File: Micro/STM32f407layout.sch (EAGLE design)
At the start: 40 parts, among them Q1 ASF, U1 LM1085IS-3.3

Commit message: Made changes to the micro board
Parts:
- removed C5, C7: 0.22uF, SparkFun-Passives:CAP0603-CAP
- removed D1: (no value), DiscreteComponents:DIODE-DO-214AC
- removed RN1: (no value), DiscreteComponents:2R-NEXBV4V
- removed T1: (no value), DiscreteComponents:FDN340P
- removed U$4: MICROUSB, Other:MICROUSB
- removed U1: LM1085IS-3.3, PowerComponents:LM1085IS-3.3
- added C10, C12: 0.22uF, rcl:C-USC0603
- added D6: (no value), DiscreteComponents:DIODE-DO-214AC
- added RN2: (no value), DiscreteComponents:2R-NEXBV4V
- added SV1, SV2, SV3: (no value), con-lsta:FE08-2
- added SV4: (no value), con-lsta:FE07-2
- added T3: FDN340P, DiscreteComponents:FDN340P
- added T4: AP1117_LIN_REG, PowerComponents:AP1117_LIN_REG
- added U$5: MICROUSB, Other:MICROUSB
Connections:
- removed net ETC_MDC: U$1G$3.PC1
- removed net ETH_CRS_DV: U$1G$1.PA7
- removed net ETH_MDIO: U$1G$1.PA2
- removed net ETH_REF_CLK: U$1G$1.PA1
- removed net ETH_RXD0: U$1G$3.PC4
- removed net ETH_RXD1: U$1G$3.PC5
- removed net ETH_TXD0: U$1G$2.PB12
- removed net ETH_TXD1: U$1G$2.PB13
- removed net ETH_TX_EN: U$1G$2.PB11
- removed net N$10: T1.D, U$4.VCC
- removed net N$16: R13.2, U$1G$4.PD13
- removed net N$19: R11.2, U$1G$4.PD11
- removed net N$22: C17.2, C18.2, U$1G$6.VSSA
- removed net N$5: D1.C, T1.S
- removed net N$6: RN1B.1, U$4.D+
- removed net N$7: RN1A.1, U$4.D-
- removed net N$8: R12.2, U$1G$4.PD12
- removed net N$9: R14.2, U$1G$4.PD14
- removed net VCC: U$6.VCC
- new net CRS_DV: SV4.7, U$1G$1.PA7
- new net MDC: SV4.5, U$1G$3.PC1
- new net MDIO: SV4.6, U$1G$1.PA2
- new net N$12: RN2A.1, U$5.D-
- new net N$24: RN2B.1, U$5.D+
- new net N$57: T3.D, U$5.VCC
- new net N$58: C12.1, D6.C, T3.S, T4.VIN
- new net PA10: SV2.14, U$1G$1.PA10
- new net PA13: U$1G$1.PA13
- new net PA14: U$1G$1.PA14
- new net PA15: U$1G$1.PA15
- new net PA5: U$1G$1.PA6
- new net PA9: SV2.13, U$1G$1.PA9
- new net PB0: U$1G$2.PB0
- new net PB1: U$1G$2.PB1
- new net PB10: U$1G$2.PB10
- new net PB14: U$1G$2.PB14
- new net PB15: U$1G$2.PB15
- new net PB2: U$1G$2.PB2
- new net PB3: U$1G$2.PB3
- new net PB4: SV1.11, U$1G$2.PB4
- new net PB9: SV1.16, U$1G$2.PB9
- new net PC0: SV3.1, U$1G$3.PC0
- new net PC10: SV1.1, U$1G$3.PC10
- new net PC11: SV1.2, U$1G$3.PC11
- new net PC12: SV1.3, U$1G$3.PC12
- new net PC13: SV3.6, U$1G$3.PC13
- new net PC14: SV3.5, U$1G$3.PC14
- new net PC15: SV3.4, U$1G$3.PC15
- new net PC2: U$1G$3.PC2
- new net PC3: U$1G$3.PC3
- new net PC6: SV2.8, U$1G$3.PC6
- new net PC7: SV2.9, U$1G$3.PC7
- new net PC8: SV2.10, U$1G$3.PC8
- new net PD0: SV1.4, U$1G$4.PD0
- new net PD1: SV1.5, U$1G$4.PD1
- new net PD10: U$1G$4.PD10
- new net PD11: R11.2, SV2.3, U$1G$4.PD11
- new net PD12: R12.2, SV2.4, U$1G$4.PD12
- new net PD13: R13.2, SV2.5, U$1G$4.PD13
- new net PD14: R14.2, SV2.6, U$1G$4.PD14
- new net PD15: SV2.7, U$1G$4.PD15
- new net PD2: SV1.6, U$1G$4.PD2
- new net PD3: SV1.7, U$1G$4.PD3
- new net PD4: SV1.8, U$1G$4.PD4
- new net PD5: SV1.9, U$1G$4.PD5
- new net PD6: SV1.10, U$1G$4.PD6
- new net PD7: U$1G$4.PD7
- new net PD8: SV2.1, U$1G$4.PD8
- new net PD9: SV2.2, U$1G$4.PD9
- new net PE0: U$1G$5.PE0
- new net PE1: U$1G$5.PE1
- new net PE10: U$1G$5.PE10
- new net PE11: U$1G$5.PE11
- new net PE12: U$1G$5.PE12
- new net PE13: U$1G$5.PE13
- new net PE14: U$1G$5.PE14
- new net PE15: U$1G$5.PE15
- new net PE2: SV3.16, U$1G$5.PE2
- new net PE3: SV3.15, U$1G$5.PE3
- new net PE4: SV3.14, U$1G$5.PE4
- new net PE5: SV3.13, U$1G$5.PE5
- new net PE6: SV3.12, U$1G$5.PE6
- new net PE7: U$1G$5.PE7
- new net PE8: U$1G$5.PE8
- new net PE9: U$1G$5.PE9
- new net PH1: SV3.2, U$1G$5.PH1
- new net REFCLK: SV4.8, U$1G$1.PA1
- new net RXD0: SV4.10, U$1G$3.PC4
- new net RXD1: SV4.9, U$1G$3.PC5
- new net TXD0: SV4.11, U$1G$2.PB12
- new net TXD1: SV4.14, U$1G$2.PB13
- new net TXEN: SV4.12, U$1G$2.PB11
- net +3V3: now also C10.1, SV2.16, SV3.10, SV3.8, SV4.1, SV4.2, T4.VOUT, U$6.VCC; no longer C7.1, U1.OUT, U1.VOUT
- net +5V: now also D6.A, T3.G; no longer C5.1, D1.A, T1.G, U1.IN
- net CAN_RX: now also SV1.12
- net CAN_TX: now also SV1.13
- net GND: now also C10.2, C12.2, C17.2, C18.2, SV2.15, SV3.11, SV3.7, SV3.9, SV4.3, SV4.4, T4.GND, U$1G$6.VSSA, U$5.GND, U$5.ID; no longer C5.2, C7.2, U$4.GND, U$4.ID, U1.ADJ/GND
- net I2C1_SCL: now also SV1.15
- net I2C1_SDA: now also SV1.14
- net I2C3_SCL: now also SV2.12
- net I2C3_SDA: now also SV2.11
- net OSC_IN: now also SV3.3
- net USB_D+: now also RN2B.2; no longer RN1B.2
- net USB_D-: now also RN2A.2; no longer RN1A.2
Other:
- note added: "Micro USB"
- note removed: "USB_D+"
- note removed: "USB_D-"
- moved on the sheet: C1, Q1, R5, R6, U$6

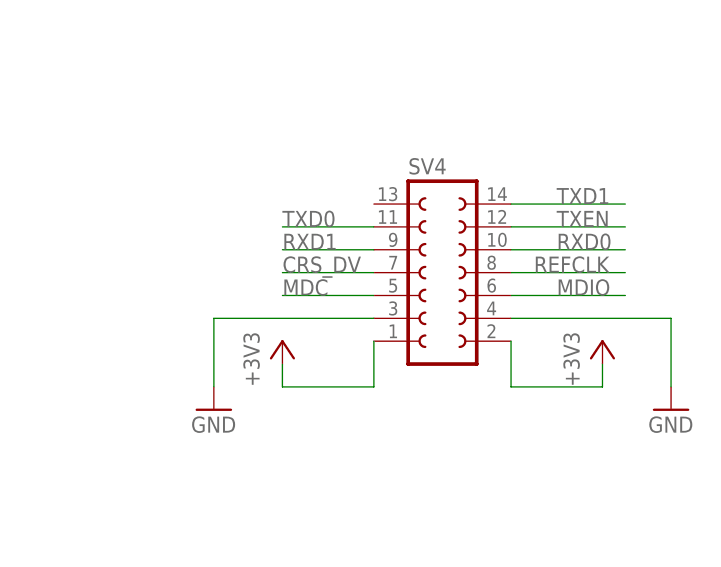
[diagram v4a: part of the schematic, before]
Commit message: Updated Board on flight
moved TXD0 pin connection to not cross transmission lines
remove PC0 so can run MDC out. If it is a clock its pretty important
that it does not go under micro
may want to move xtal, bit far away probably wont be a problem but hf
signals do not like distance and things inbetween them
check via usage, use different ones , may want to stick to 1 size
move i2c resistors to bottom, connected them to 3v3
are linear regs noisey or is that switching? pretty sure it is switching
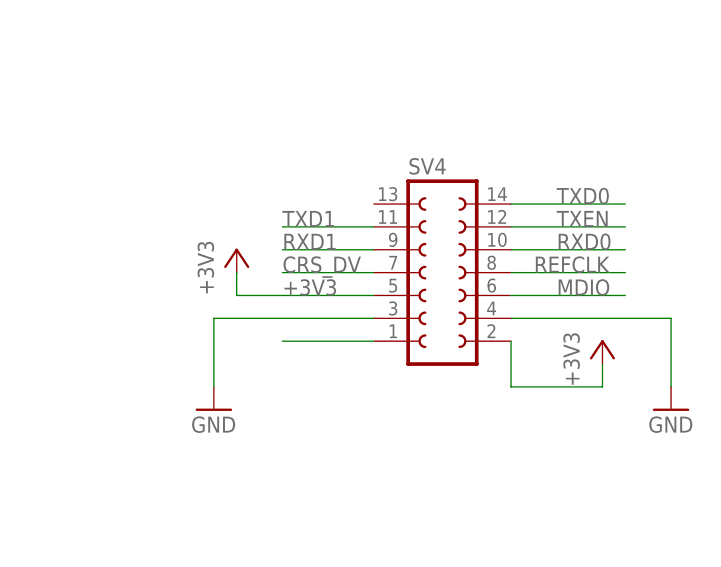
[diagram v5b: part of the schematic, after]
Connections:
- net +3V3: now also SV4.5; no longer SV4.1
- net MDC: now also SV4.1; no longer SV4.5
- net TXD0: now also SV4.14; no longer SV4.11
- net TXD1: now also SV4.11; no longer SV4.14
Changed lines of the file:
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@@
 <?xml version="1.0" encoding="utf-8"?>
 <!DOCTYPE eagle SYSTEM "eagle.dtd">
-<eagle version="7.2.0">
+<eagle version="7.4.0">
 <drawing>
 <settings>
@@
 <instance part="GND4" gate="1" x="866.14" y="370.84"/>
 <instance part="GND7" gate="1" x="815.34" y="370.84"/>
-<instance part="+3V12" gate="G$1" x="822.96" y="378.46"/>
+<instance part="+3V12" gate="G$1" x="817.88" y="388.62"/>
 <instance part="+3V13" gate="G$1" x="858.52" y="378.46"/>
 </instances>
@@
 </segment>
 <segment>
-<pinref part="+3V12" gate="G$1" pin="+3V3"/>
-<wire x1="822.96" y1="375.92" x2="822.96" y2="373.38" width="0.1524" layer="91"/>
-<pinref part="SV4" gate="G$1" pin="1"/>
-<wire x1="822.96" y1="373.38" x2="833.12" y2="373.38" width="0.1524" layer="91"/>
-<wire x1="833.12" y1="373.38" x2="833.12" y2="378.46" width="0.1524" layer="91"/>
-</segment>
-<segment>
 <pinref part="SV4" gate="G$1" pin="2"/>
 <wire x1="848.36" y1="378.46" x2="848.36" y2="373.38" width="0.1524" layer="91"/>
@@
 <wire x1="848.36" y1="373.38" x2="858.52" y2="373.38" width="0.1524" layer="91"/>
 <wire x1="858.52" y1="373.38" x2="858.52" y2="375.92" width="0.1524" layer="91"/>
+</segment>
+<segment>
+<pinref part="SV4" gate="G$1" pin="5"/>
+<wire x1="833.12" y1="383.54" x2="817.88" y2="383.54" width="0.1524" layer="91"/>
+<label x="822.96" y="383.54" size="1.778" layer="95"/>
+<pinref part="+3V12" gate="G$1" pin="+3V3"/>
+<wire x1="817.88" y1="383.54" x2="817.88" y2="386.08" width="0.1524" layer="91"/>
 </segment>
 </net>
@@
 <net name="TXD0" class="0">
 <segment>
+<pinref part="U$1" gate="G$2" pin="PB12"/>
+<wire x1="439.42" y1="292.1" x2="459.74" y2="292.1" width="0.1524" layer="91"/>
+<label x="452.12" y="292.1" size="1.778" layer="95"/>
+</segment>
+<segment>
+<pinref part="SV4" gate="G$1" pin="14"/>
+<wire x1="848.36" y1="393.7" x2="861.06" y2="393.7" width="0.1524" layer="91"/>
+<label x="853.44" y="393.7" size="1.778" layer="95"/>
+</segment>
+</net>
+<net name="TXD1" class="0">
+<segment>
+<pinref part="U$1" gate="G$2" pin="PB13"/>
+<wire x1="439.42" y1="287.02" x2="459.74" y2="287.02" width="0.1524" layer="91"/>
+<label x="452.12" y="287.02" size="1.778" layer="95"/>
+</segment>
+<segment>
 <pinref part="SV4" gate="G$1" pin="11"/>
 <wire x1="833.12" y1="391.16" x2="822.96" y2="391.16" width="0.1524" layer="91"/>
 <label x="822.96" y="391.16" size="1.778" layer="95"/>
 </segment>
-<segment>
-<pinref part="U$1" gate="G$2" pin="PB12"/>
-<wire x1="439.42" y1="292.1" x2="459.74" y2="292.1" width="0.1524" layer="91"/>
-<label x="452.12" y="292.1" size="1.778" layer="95"/>
-</segment>
-</net>
-<net name="TXD1" class="0">
-<segment>
-<pinref part="SV4" gate="G$1" pin="14"/>
-<wire x1="848.36" y1="393.7" x2="861.06" y2="393.7" width="0.1524" layer="91"/>
-<label x="853.44" y="393.7" size="1.778" layer="95"/>
-</segment>
-<segment>
-<pinref part="U$1" gate="G$2" pin="PB13"/>
-<wire x1="439.42" y1="287.02" x2="459.74" y2="287.02" width="0.1524" layer="91"/>
-<label x="452.12" y="287.02" size="1.778" layer="95"/>
-</segment>
 </net>
 <net name="MDC" class="0">
-<segment>
-<pinref part="SV4" gate="G$1" pin="5"/>
-<wire x1="833.12" y1="383.54" x2="822.96" y2="383.54" width="0.1524" layer="91"/>
-<label x="822.96" y="383.54" size="1.778" layer="95"/>
-</segment>
 <segment>
 <pinref part="U$1" gate="G$3" pin="PC1"/>
@@
 <label x="586.74" y="505.46" size="1.778" layer="95"/>
 </segment>
-</net>
+<segment>
+<pinref part="SV4" gate="G$1" pin="1"/>
+<wire x1="822.96" y1="378.46" x2="833.12" y2="378.46" width="0.1524" layer="91"/>
+</segment>
+</net>

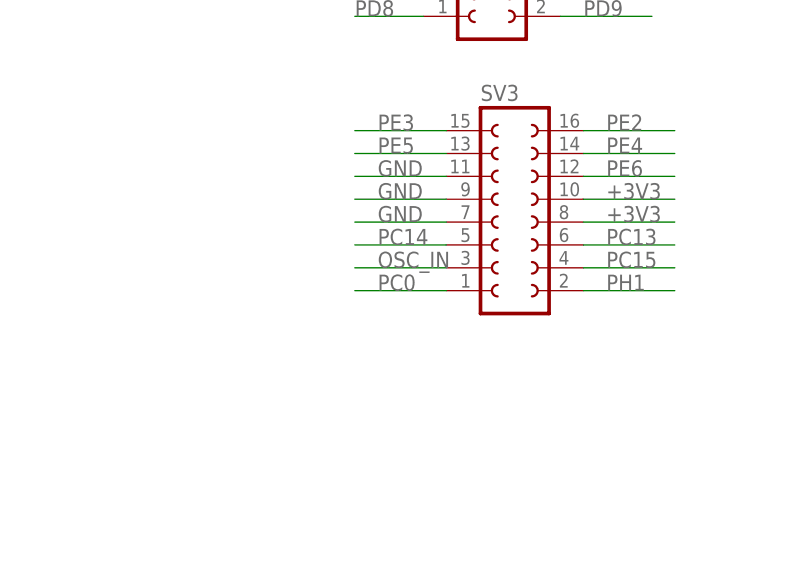
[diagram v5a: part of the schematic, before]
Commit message: Holiday Update 1
Connected extra capacitors, changed PC0 to GND for now, May route to
better pinout later. Added GND planes made sure no unrouted
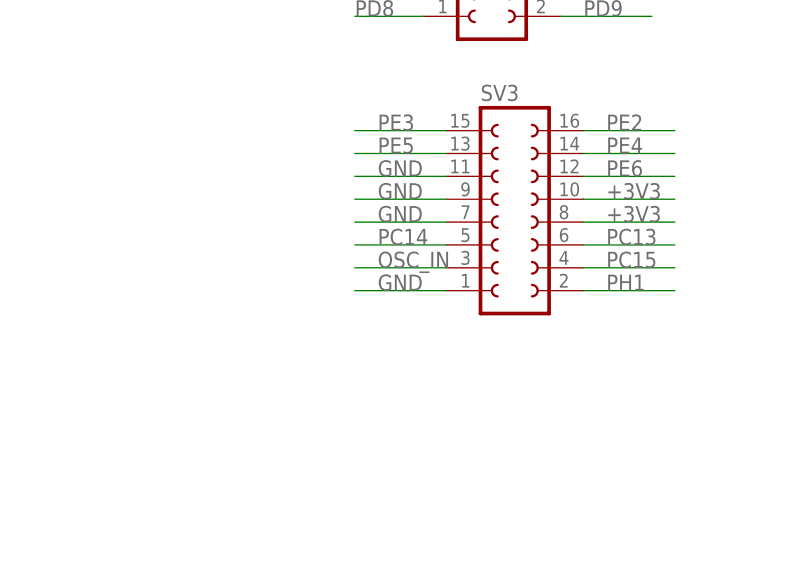
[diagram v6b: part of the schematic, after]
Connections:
- net GND: now also SV3.1
- net PC0: no longer SV3.1
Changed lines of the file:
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@@
 <wire x1="866.14" y1="381" x2="866.14" y2="373.38" width="0.1524" layer="91"/>
+</segment>
+<segment>
+<pinref part="SV3" gate="G$1" pin="1"/>
+<wire x1="497.84" y1="154.94" x2="487.68" y2="154.94" width="0.1524" layer="91"/>
+<label x="490.22" y="154.94" size="1.778" layer="95"/>
 </segment>
 </net>
@@
 <label x="586.74" y="510.54" size="1.778" layer="95"/>
 </segment>
-<segment>
-<pinref part="SV3" gate="G$1" pin="1"/>
-<wire x1="497.84" y1="154.94" x2="487.68" y2="154.94" width="0.1524" layer="91"/>
-<label x="490.22" y="154.94" size="1.778" layer="95"/>
-</segment>
-</net>
+</net>
